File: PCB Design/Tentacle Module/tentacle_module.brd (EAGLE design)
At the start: 101.6 x 30.5 mm, 58 parts, among them IC1 5.0V, IC3 3.3V, T1 NTD5867NL, T2 NTD5867NL, T3 NTD5867NL, T4 NTD5867NL, U1 OKR-T/10-W12, X3 RJ45-8X, X4 RJ45-8X

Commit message: Changed Tentacle module
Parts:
- added DRILEGEND: (no value), drilegend:DRILEGEND
- moved R13 3.86 mm to (93.6, 22.4)
- moved LED5 3.42 mm to (93.2, 26.9), turned to 90 degrees
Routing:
- net +12V: track 43.5 -> 58.0 mm
- net PWR_LED_GND: track 0.32 -> 3.71 mm
- net N$10: track 1.75 -> 2.45 mm

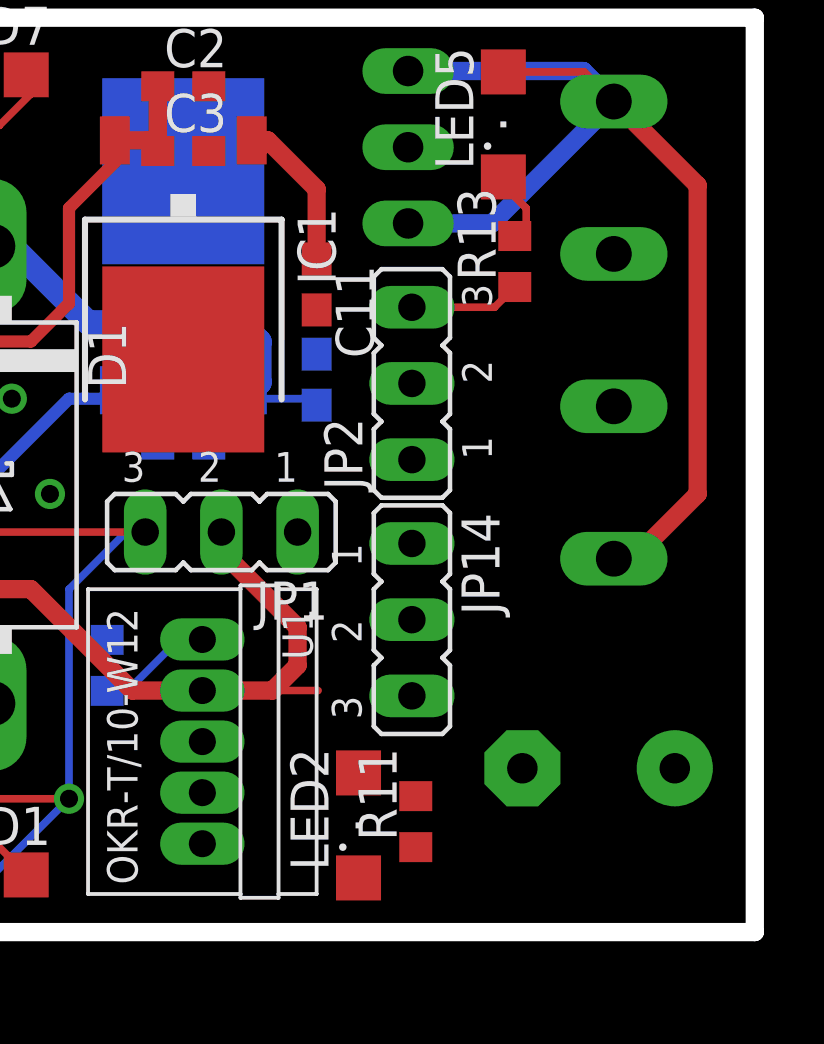
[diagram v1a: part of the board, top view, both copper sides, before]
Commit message: Finished updating the Tentacle board
not polished yet though
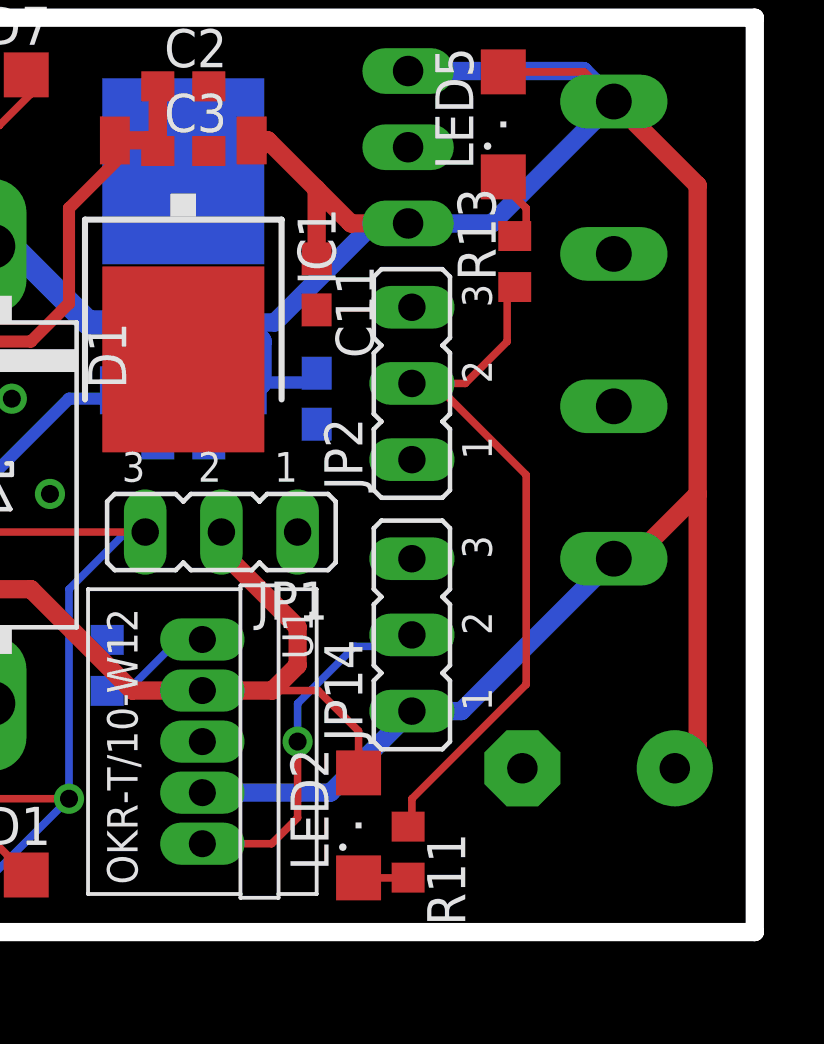
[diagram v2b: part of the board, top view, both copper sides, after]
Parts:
- moved R11 1.05 mm to (90.0, 2.67), turned to 270 degrees
- moved C10 0.63 mm to (87.0, 17.8), turned to 270 degrees
- moved JP14 0.51 mm to (90.2, 9.91), turned to 90 degrees
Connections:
- net +12V: now also JP14.1; no longer JP14.3
- net GND: now also JP14.3, JP2.1; no longer JP14.1, JP2.2
- net PWR_LED_GND: now also JP2.2; no longer JP2.3
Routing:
- net +12V: track 58.0 -> 94.6 mm
- net PWR_LED_GND: track 3.71 -> 24.1 mm
- net 5V_ENABLE: track 0.00 -> 12.1 mm, vias 0 -> 1
- net +5V_HI-PWR: track 96.7 -> 100.0 mm
- net N$7: track 0.00 -> 1.66 mm
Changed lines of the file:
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@@
 <?xml version="1.0" encoding="utf-8"?>
 <!DOCTYPE eagle SYSTEM "eagle.dtd">
-<eagle version="7.0.0">
+<eagle version="7.1.0">
 <drawing>
 <settings>
@@
 <layer number="19" name="Unrouted" color="6" fill="1" visible="yes" active="yes"/>
 <layer number="20" name="Dimension" color="15" fill="1" visible="yes" active="yes"/>
-<layer number="21" name="tPlace" color="7" fill="1" visible="yes" active="yes"/>
-<layer number="22" name="bPlace" color="7" fill="1" visible="yes" active="yes"/>
+<layer number="21" name="tPlace" color="7" fill="1" visible="no" active="yes"/>
+<layer number="22" name="bPlace" color="7" fill="1" visible="no" active="yes"/>
 <layer number="23" name="tOrigins" color="15" fill="1" visible="yes" active="yes"/>
 <layer number="24" name="bOrigins" color="15" fill="1" visible="yes" active="yes"/>
@@
 <element name="JP13" library="CBLA_Test_bed_Library" package="1X08" value="" x="26.67" y="2.54"/>
 <element name="U1" library="CBLA_Test_bed_Library" package="OKR-C90" value="OKR-T/10-W12" x="83.185" y="6.35" rot="R270"/>
-<element name="JP14" library="jumper" package="JP2" value="" x="90.17" y="10.414" rot="R270"/>
+<element name="JP14" library="jumper" package="JP2" value="" x="90.17" y="9.906" rot="R90"/>
 <element name="R10" library="CBLA_Test_bed_Library" package="R0603" value="267" x="80.01" y="8.89" rot="MR270"/>
 <element name="LED2" library="led" package="SML1206" value="" x="88.392" y="3.556" rot="R90"/>
-<element name="R11" library="CBLA_Test_bed_Library" package="R0603" value="470" x="90.297" y="3.683" rot="R90"/>
+<element name="R11" library="CBLA_Test_bed_Library" package="R0603" value="470" x="90.043" y="2.667" rot="R270"/>
 <element name="JP2" library="jumper" package="JP2" value="" x="90.17" y="18.288" rot="R90"/>
 <element name="C3" library="rcl" package="C0603" value="100nF" x="82.55" y="26.035"/>
@@
 <element name="C8" library="rcl" package="C0603" value="100nF" x="53.975" y="7.62" rot="MR0"/>
 <element name="C9" library="rcl" package="C0603" value="100nF" x="59.055" y="22.225" rot="MR180"/>
-<element name="C10" library="rcl" package="C0603" value="10uF" x="86.995" y="18.415" rot="MR90"/>
+<element name="C10" library="rcl" package="C0603" value="10uF" x="86.995" y="17.78" rot="MR270"/>
 <element name="IC3" library="CBLA_Test_bed_Library" package="DPACK" value="3.3V" x="82.55" y="22.86" rot="MR0">
 <attribute name="MFN" value="NCP1117DT33" x="82.55" y="22.86" size="1.778" layer="28" rot="MR0" display="off"/>
@@
 <contactref element="X1" pad="1"/>
 <contactref element="U1" pad="VIN"/>
-<contactref element="JP14" pad="3"/>
 <contactref element="LED5" pad="A"/>
 <contactref element="X1" pad="4"/>
@@
 <contactref element="C11" pad="1"/>
 <wire x1="84.836" y1="26.416" x2="84.83" y2="26.39" width="0.254" layer="1"/>
-<wire x1="85.09" y1="17.78" x2="86.868" y2="17.78" width="0.254" layer="16"/>
 <wire x1="84.836" y1="18.034" x2="85.09" y2="17.78" width="0.254" layer="16"/>
-<wire x1="86.868" y1="17.78" x2="86.995" y2="17.565" width="0.254" layer="16"/>
 <wire x1="84.836" y1="18.034" x2="84.83" y2="18.06" width="0.254" layer="16"/>
-<wire x1="87.122" y1="17.78" x2="86.995" y2="17.565" width="0.254" layer="16"/>
 <wire x1="84.83" y1="26.39" x2="85.37" y2="26.39" width="0.6096" layer="1"/>
 <wire x1="85.37" y1="26.39" x2="86.995" y2="24.765" width="0.6096" layer="1"/>
@@
 <wire x1="99.695" y1="14.605" x2="99.695" y2="24.892" width="0.6096" layer="1"/>
 <wire x1="99.695" y1="24.892" x2="96.901" y2="27.686" width="0.6096" layer="1"/>
-<wire x1="90.043" y1="23.622" x2="86.995" y2="24.765" width="0" layer="19" extent="1-1"/>
-<wire x1="84.455" y1="20.32" x2="86.995" y2="22.44" width="0" layer="19" extent="1-16"/>
-<wire x1="98.933" y1="5.461" x2="97.536" y2="12.446" width="0" layer="19" extent="1-1"/>
-<wire x1="90.17" y1="7.874" x2="96.901" y2="12.446" width="0" layer="19" extent="1-1"/>
-<wire x1="83.185" y1="4.6482" x2="90.17" y2="7.874" width="0" layer="19" extent="1-1"/>
+<wire x1="98.933" y1="5.461" x2="99.695" y2="6.223" width="0.6096" layer="1"/>
+<wire x1="99.695" y1="6.223" x2="99.695" y2="14.605" width="0.6096" layer="1"/>
+<wire x1="90.043" y1="23.622" x2="88.138" y2="23.622" width="0.6096" layer="1"/>
+<wire x1="88.138" y1="23.622" x2="86.995" y2="24.765" width="0.6096" layer="1"/>
+<wire x1="84.455" y1="20.32" x2="85.598" y2="20.32" width="0.6096" layer="16"/>
+<wire x1="85.598" y1="20.32" x2="88.9" y2="23.622" width="0.6096" layer="16"/>
+<wire x1="88.9" y1="23.622" x2="90.043" y2="23.622" width="0.6096" layer="16"/>
+<contactref element="JP14" pad="1"/>
+<wire x1="83.185" y1="4.6482" x2="87.4522" y2="4.6482" width="0.6096" layer="16"/>
+<wire x1="87.4522" y1="4.6482" x2="90.17" y2="7.366" width="0.6096" layer="16"/>
+<wire x1="90.17" y1="7.366" x2="91.821" y2="7.366" width="0.6096" layer="16"/>
+<wire x1="91.821" y1="7.366" x2="96.901" y2="12.446" width="0.6096" layer="16"/>
+<wire x1="85.09" y1="18.32" x2="86.685" y2="18.32" width="0.4064" layer="16"/>
+<wire x1="86.685" y1="18.32" x2="86.995" y2="18.63" width="0.4064" layer="16"/>
 </signal>
 <signal name="+5V">
@@
 <contactref element="X1" pad="3"/>
 <contactref element="JP13" pad="7"/>
-<contactref element="JP14" pad="1"/>
 <contactref element="U1" pad="GND"/>
 <contactref element="R10" pad="1"/>
@@
 <contactref element="C11" pad="2"/>
 <contactref element="C10" pad="2"/>
-<contactref element="JP2" pad="2"/>
 <contactref element="D1" pad="A"/>
 <contactref element="X1" pad="2"/>
@@
 <via x="57.15" y="26.035" extent="1-16" drill="0.6"/>
 <contactref element="JP3" pad="2"/>
+<contactref element="JP2" pad="1"/>
+<contactref element="JP14" pad="3"/>
 </signal>
 <signal name="SMA1_OUT-">
@@
 <wire x1="58.205" y1="22.225" x2="58.205" y2="24.59" width="0.6096" layer="16"/>
 <wire x1="58.205" y1="24.59" x2="59.65" y2="26.035" width="0.6096" layer="16"/>
-<wire x1="87.0432" y1="8.0518" x2="88.392" y2="5.306" width="0" layer="19" extent="1-1"/>
+<wire x1="88.392" y1="5.306" x2="88.392" y2="6.703" width="0.254" layer="1"/>
+<wire x1="88.392" y1="6.703" x2="87.0432" y2="8.0518" width="0.254" layer="1"/>
 </signal>
 <signal name="TEST_LED_V+">
@@
 <contactref element="U1" pad="ON/OFF"/>
 <contactref element="JP14" pad="2"/>
-<wire x1="83.185" y1="2.9464" x2="90.17" y2="10.414" width="0" layer="19" extent="1-1"/>
+<wire x1="83.185" y1="2.9464" x2="85.4964" y2="2.9464" width="0.254" layer="1"/>
+<wire x1="85.4964" y1="2.9464" x2="86.36" y2="3.81" width="0.254" layer="1"/>
+<wire x1="86.36" y1="3.81" x2="86.36" y2="6.35" width="0.254" layer="1"/>
+<via x="86.36" y="6.35" extent="1-16" drill="0.6"/>
+<wire x1="86.36" y1="6.35" x2="86.36" y2="7.62" width="0.254" layer="16"/>
+<wire x1="86.36" y1="7.62" x2="88.265" y2="9.525" width="0.254" layer="16"/>
+<wire x1="88.265" y1="9.525" x2="89.789" y2="9.525" width="0.254" layer="16"/>
+<wire x1="89.789" y1="9.525" x2="90.17" y2="9.906" width="0.254" layer="16"/>
 </signal>
 <signal name="N$6">
@@
 <contactref element="R11" pad="2"/>
 <contactref element="LED2" pad="C"/>
-<wire x1="88.392" y1="1.806" x2="90.297" y2="4.533" width="0" layer="19" extent="1-1"/>
+<wire x1="88.392" y1="1.806" x2="90.032" y2="1.806" width="0.254" layer="1"/>
+<wire x1="90.032" y1="1.806" x2="90.043" y2="1.817" width="0.254" layer="1"/>
 </signal>
 <signal name="PWR_LED_GND">
+<contactref element="R11" pad="1"/>
+<contactref element="JP2" pad="2"/>
 <contactref element="R13" pad="1"/>
-<contactref element="R11" pad="1"/>
-<contactref element="JP2" pad="3"/>
-<wire x1="90.17" y1="20.828" x2="92.925" y2="20.828" width="0.254" layer="1"/>
-<wire x1="92.925" y1="20.828" x2="93.599" y2="21.502" width="0.254" layer="1"/>
-<wire x1="90.297" y1="2.833" x2="90.17" y2="20.828" width="0" layer="19" extent="1-1"/>
+<wire x1="90.17" y1="18.288" x2="91.948" y2="18.288" width="0.254" layer="1"/>
+<wire x1="91.948" y1="18.288" x2="93.345" y2="19.685" width="0.254" layer="1"/>
+<wire x1="93.345" y1="19.685" x2="93.345" y2="21.248" width="0.254" layer="1"/>
+<wire x1="93.345" y1="21.248" x2="93.599" y2="21.502" width="0.254" layer="1"/>
+<wire x1="90.17" y1="18.288" x2="90.932" y2="18.288" width="0.254" layer="1"/>
+<wire x1="90.932" y1="18.288" x2="93.98" y2="15.24" width="0.254" layer="1"/>
+<wire x1="93.98" y1="15.24" x2="93.98" y2="8.255" width="0.254" layer="1"/>
+<wire x1="93.98" y1="8.255" x2="90.17" y2="4.445" width="0.254" layer="1"/>
+<wire x1="90.17" y1="4.445" x2="90.17" y2="3.644" width="0.254" layer="1"/>
+<wire x1="90.17" y1="3.644" x2="90.043" y2="3.517" width="0.254" layer="1"/>
 </signal>
 <signal name="N$12">

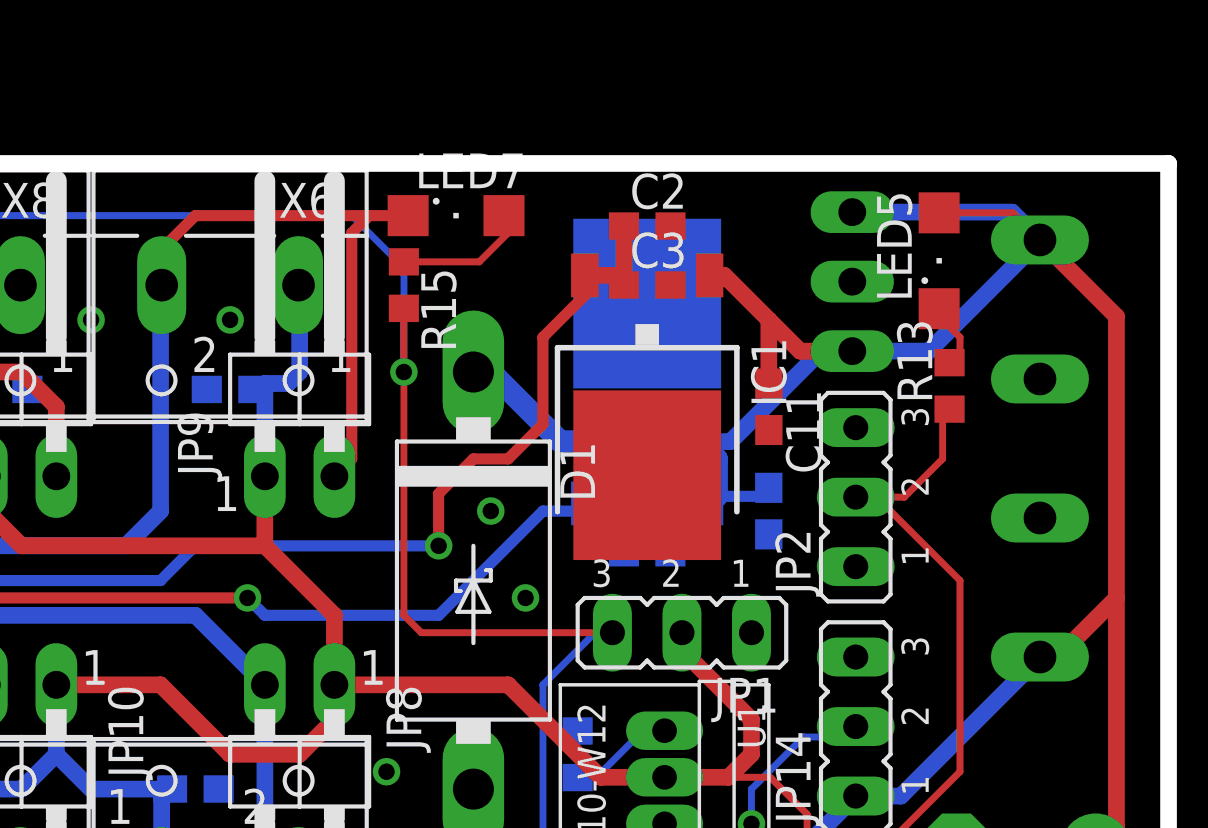
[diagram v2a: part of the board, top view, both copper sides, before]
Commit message: removed the unnecesssary by-pass cap by the v-reg
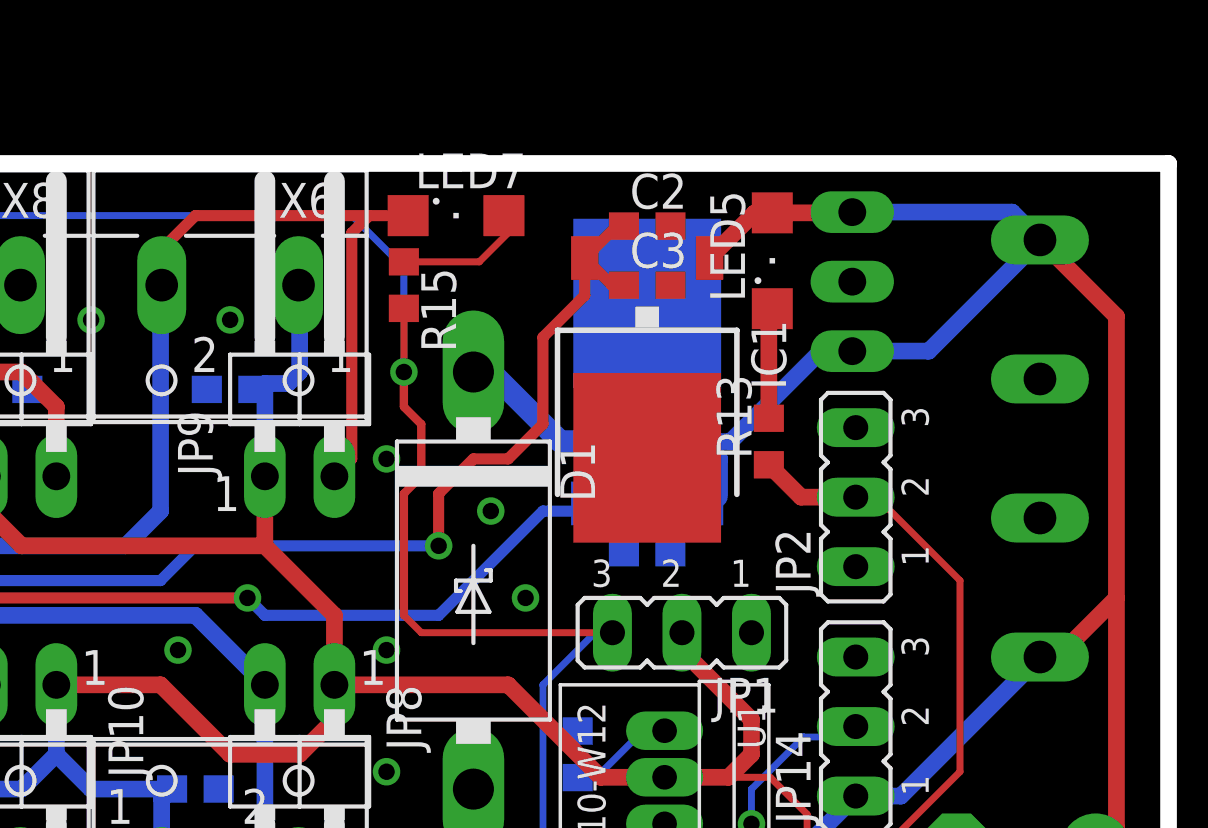
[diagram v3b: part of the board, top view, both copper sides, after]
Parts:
- removed C10, C11: 10uF, rcl:C0603
- C6, C7, C8, C9: value 100nF -> 10uF
- IC1: value 5.0V -> MC7805BDTRKG; device CBLA_Test_bed_Library:DPACK -> CBLA_Test_bed_Library:DPACK_3
- IC2: value 3.3V -> UA78M33CKVU
- moved R13 6.91 mm to (87.0, 20.3)
- moved LED5 6.10 mm to (87.1, 26.9)
- moved IC1 0.64 mm to (82.5, 22.2)
- renumbered IC3 to IC2
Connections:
- net +12V: no longer C10.1, C11.1
- net GND: now also IC1.4; no longer C10.2, C11.2, IC1.2
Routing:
- net +12V: track 94.6 -> 85.0 mm
- net PWR_LED_GND: track 24.1 -> 22.1 mm
- net N$10: track 2.45 -> 4.06 mm
- net +5V: track 101.0 -> 101.6 mm
- net TEST_LED_V+: track 93.4 -> 93.9 mm
- net GND: vias 23 -> 26
